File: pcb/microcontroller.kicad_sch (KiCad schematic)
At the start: 23 parts, among them J1 TC2030, U3 74HCT541, U4 STM32F103C8T6, U5 SN65HVD230, Y1 8MHz

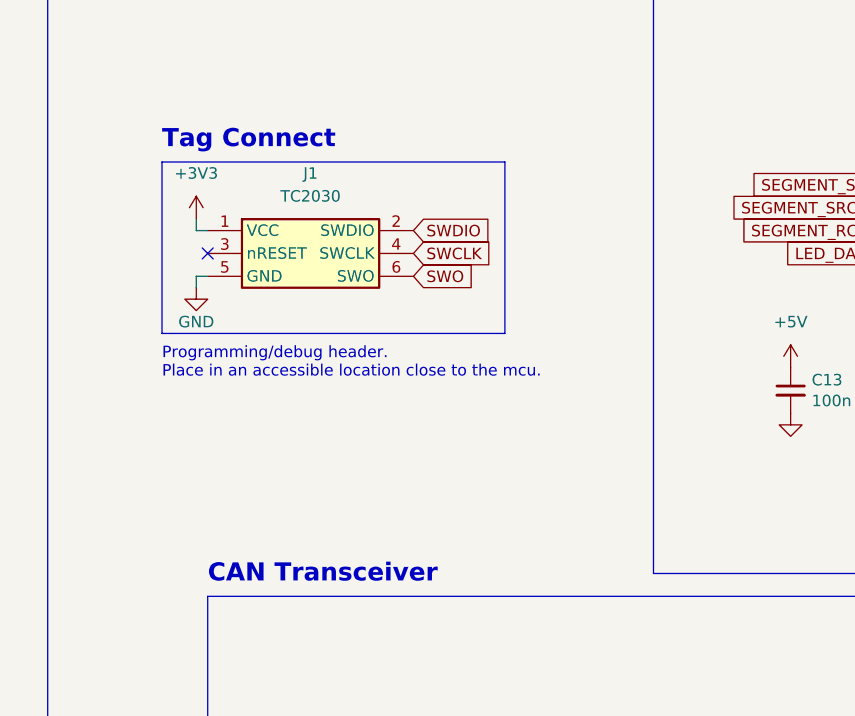
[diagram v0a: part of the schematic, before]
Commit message: Laid out and routed PCB
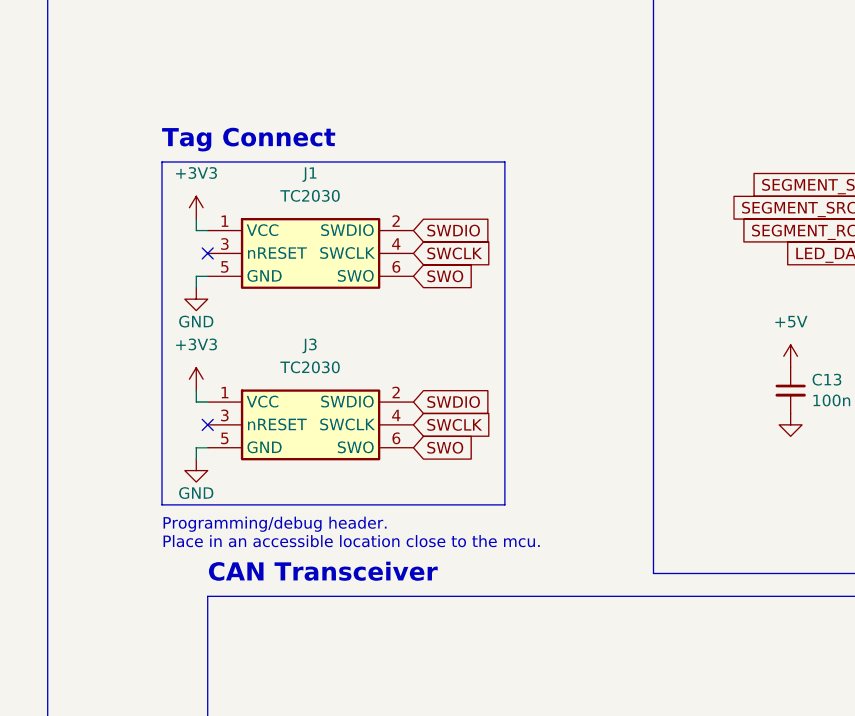
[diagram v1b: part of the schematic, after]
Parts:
- added J3: TC2030, Connector:Tag-Connect_TC2030-IDC-NL_2x03_P1.27mm_Vertical, symbol TC2030:TC2030
- C16, C19: footprint (none) -> Capacitor_SMD:C_0402_1005Metric
- D7: footprint (none) -> Package_TO_SOT_SMD:SOT-323_SC-70
- R5, R6: footprint (none) -> Resistor_SMD:R_0805_2012Metric
- U3: footprint (none) -> Package_SO:SSOP-20_4.4x6.5mm_P0.65mm
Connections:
- net +3V3: now also J3.1 (VCC)
- net GND: now also J3.5 (GND)
- net SWCLK: now also J3.4 (SWCLK)
- net SWDIO: now also J3.2 (SWDIO)
- net SWO: now also J3.6 (SWO)
- no-connect marks 19 -> 20
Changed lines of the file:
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@@
   (junction (at 86.36 66.04) (diameter 0) (color 0 0 0 0)
   )
+  (no_connect (at 152.4 74.93))
   (no_connect (at 257.81 66.04))
   (no_connect (at 71.12 92.71))
@@
     (stroke (width 0) (type default) (color 0 0 0 0))
   )
+  (wire (pts (xy 151.13 72.39) (xy 151.13 71.12))
+    (stroke (width 0) (type default) (color 0 0 0 0))
+  )
   (wire (pts (xy 99.06 36.83) (xy 102.87 36.83))
     (stroke (width 0) (type default) (color 0 0 0 0))
@@
     (stroke (width 0) (type default) (color 0 0 0 0))
   )
+  (wire (pts (xy 152.4 72.39) (xy 151.13 72.39))
+    (stroke (width 0) (type default) (color 0 0 0 0))
+  )
   (wire (pts (xy 88.9 66.04) (xy 91.44 66.04))
     (stroke (width 0) (type default) (color 0 0 0 0))
@@
     (stroke (width 0) (type default) (color 0 0 0 0))
   )
+  (wire (pts (xy 151.13 77.47) (xy 152.4 77.47))
+    (stroke (width 0) (type default) (color 0 0 0 0))
+  )
   (polyline (pts (xy 224.79 101.6) (xy 224.79 147.32))
     (stroke (width 0) (type default) (color 0 0 0 0))
@@
     (stroke (width 0) (type default) (color 0 0 0 0))
   )
-  (polyline (pts (xy 147.32 64.77) (xy 185.42 64.77))
+  (polyline (pts (xy 147.32 83.82) (xy 185.42 83.82))
     (stroke (width 0) (type default) (color 0 0 0 0))
   )
@@
     (stroke (width 0) (type default) (color 0 0 0 0))
   )
+  (wire (pts (xy 151.13 78.74) (xy 151.13 77.47))
+    (stroke (width 0) (type default) (color 0 0 0 0))
+  )
   (wire (pts (xy 152.4 53.34) (xy 151.13 53.34))
     (stroke (width 0) (type default) (color 0 0 0 0))
@@
     (stroke (width 0) (type default) (color 0 0 0 0))
   )
-  (polyline (pts (xy 185.42 45.72) (xy 185.42 64.77))
+  (polyline (pts (xy 185.42 45.72) (xy 185.42 83.82))
     (stroke (width 0) (type default) (color 0 0 0 0))
   )
@@
     (stroke (width 0) (type default) (color 0 0 0 0))
   )
-  (polyline (pts (xy 147.32 64.77) (xy 147.32 45.72))
+  (polyline (pts (xy 147.32 83.82) (xy 147.32 45.72))
     (stroke (width 0) (type default) (color 0 0 0 0))
   )
@@
   )
   (text "Programming/debug header.\nPlace in an accessible location close to the mcu."
-    (at 147.32 69.85 0)
+    (at 147.32 88.9 0)
     (effects (font (size 1.27 1.27)) (justify left bottom))
   )
@@
     )
   )
+  (global_label "SWCLK" (shape input) (at 175.26 74.93 0) (fields_autoplaced)
+    (effects (font (size 1.27 1.27)) (justify left))
+    (property "Intersheet References" "${INTERSHEET_REFS}" (id 0) (at -62.23 -64.77 0)
+      (effects (font (size 1.27 1.27)) hide)
+    )
+  )
   (global_label "DIAL8" (shape input) (at 71.12 100.33 180) (fields_autoplaced)
     (effects (font (size 1.27 1.27)) (justify right))
@@
     )
   )
+  (global_label "SWDIO" (shape input) (at 175.26 72.39 0) (fields_autoplaced)
+    (effects (font (size 1.27 1.27)) (justify left))
+    (property "Intersheet References" "${INTERSHEET_REFS}" (id 0) (at -62.23 -64.77 0)
+      (effects (font (size 1.27 1.27)) hide)
+    )
+  )
   (global_label "DIAL9" (shape input) (at 71.12 102.87 180) (fields_autoplaced)
     (effects (font (size 1.27 1.27)) (justify right))
@@
     (effects (font (size 1.27 1.27)) (justify left))
     (property "Intersheet References" "${INTERSHEET_REFS}" (id 0) (at 250.2445 115.4906 0)
+      (effects (font (size 1.27 1.27)) (justify left) hide)
+    )
+  )
+  (global_label "SWO" (shape input) (at 175.26 77.47 0) (fields_autoplaced)
+    (effects (font (size 1.27 1.27)) (justify left))
+    (property "Intersheet References" "${INTERSHEET_REFS}" (id 0) (at 379.73 -34.29 0)
       (effects (font (size 1.27 1.27)) (justify left) hide)
     )
@@
       (effects (font (size 1.27 1.27)) (justify left))
     )
-    (property "Footprint" "" (id 2) (at 236.22 120.65 0)
+    (property "Footprint" "Package_TO_SOT_SMD:SOT-323_SC-70" (id 2) (at 236.22 120.65 0)
       (effects (font (size 1.27 1.27)) hide)
     )
@@
     (pin "1")
   )
+  (symbol (lib_id "power:+3V3") (at 151.13 71.12 0) (unit 1)
+    (in_bom yes) (on_board yes) (fields_autoplaced)
+    (property "Reference" "#PWR013" (id 0) (at 151.13 74.93 0)
+      (effects (font (size 1.27 1.27)) hide)
+    )
+    (property "Value" "+3V3" (id 1) (at 151.13 66.04 0))
+    (property "Footprint" "" (id 2) (at 151.13 71.12 0)
+      (effects (font (size 1.27 1.27)) hide)
+    )
+    (property "Datasheet" "" (id 3) (at 151.13 71.12 0)
+      (effects (font (size 1.27 1.27)) hide)
+    )
+    (pin "1")
+  )
   (symbol (lib_id "Device:C_Small") (at 217.17 71.12 0) (unit 1)
     (in_bom yes) (on_board yes)
@@
       (effects (font (size 1.27 1.27)) (justify left))
     )
-    (property "Footprint" "" (id 2) (at 212.09 119.38 0)
+    (property "Footprint" "Resistor_SMD:R_0805_2012Metric" (id 2) (at 212.09 119.38 0)
       (effects (font (size 1.27 1.27)) hide)
     )
@@
       (effects (font (size 1.27 1.27)) (justify left))
     )
-    (property "Footprint" "" (id 2) (at 245.11 60.96 0)
+    (property "Footprint" "Package_SO:SSOP-20_4.4x6.5mm_P0.65mm" (id 2) (at 245.11 60.96 0)
       (effects (font (size 1.27 1.27)) hide)
     )
@@
       (effects (font (size 1.27 1.27)) (justify left))
     )
-    (property "Footprint" "" (id 2) (at 236.22 110.49 0)
+    (property "Footprint" "Capacitor_SMD:C_0402_1005Metric" (id 2) (at 236.22 110.49 0)
       (effects (font (size 1.27 1.27)) hide)
     )
@@
       (effects (font (size 1.27 1.27)) (justify left))
     )
-    (property "Footprint" "" (id 2) (at 236.22 138.43 0)
+    (property "Footprint" "Capacitor_SMD:C_0402_1005Metric" (id 2) (at 236.22 138.43 0)
       (effects (font (size 1.27 1.27)) hide)
     )
@@
     (pin "1")
   )
+  (symbol (lib_id "TC2030:TC2030") (at 163.83 74.93 0) (unit 1)
+    (in_bom no) (on_board yes) (fields_autoplaced)
+    (property "Reference" "J3" (id 0) (at 163.83 66.04 0))
+    (property "Value" "TC2030" (id 1) (at 163.83 68.58 0))
+    (property "Footprint" "Connector:Tag-Connect_TC2030-IDC-NL_2x03_P1.27mm_Vertical" (id 2) (at 163.83 69.85 0)
+      (effects (font (size 1.27 1.27)) hide)
+    )
+    (property "Datasheet" "" (id 3) (at 163.83 69.85 0)
+      (effects (font (size 1.27 1.27)) hide)
+    )
+    (pin "1")
+    (pin "2")
+    (pin "3")
+    (pin "4")
+    (pin "5")
+    (pin "6")
+  )
   (symbol (lib_id "Device:C_Small") (at 158.75 124.46 0) (unit 1)
     (in_bom yes) (on_board yes)
@@
       (effects (font (size 1.27 1.27)) (justify left))
     )
-    (property "Footprint" "" (id 2) (at 212.09 129.54 0)
+    (property "Footprint" "Resistor_SMD:R_0805_2012Metric" (id 2) (at 212.09 129.54 0)
       (effects (font (size 1.27 1.27)) hide)
     )
@@
       (effects (font (size 1.27 1.27)) hide)
     )
+    (pin "1")
+  )
+  (symbol (lib_id "power:GND") (at 151.13 78.74 0) (unit 1)
+    (in_bom yes) (on_board yes)
+    (property "Reference" "#PWR071" (id 0) (at 151.13 85.09 0)
+      (effects (font (size 1.27 1.27)) hide)
+    )
+    (property "Value" "GND" (id 1) (at 151.13 82.55 0))
+    (property "Footprint" "" (id 2) (at 151.13 78.74 0)
+      (effects (font (size 1.27 1.27)) hide)
+    )
+    (property "Datasheet" "" (id 3) (at 151.13 78.74 0)
+      (effects (font (size 1.27 1.27)) hide)
+    )
